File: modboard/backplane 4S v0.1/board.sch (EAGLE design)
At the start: 20 parts

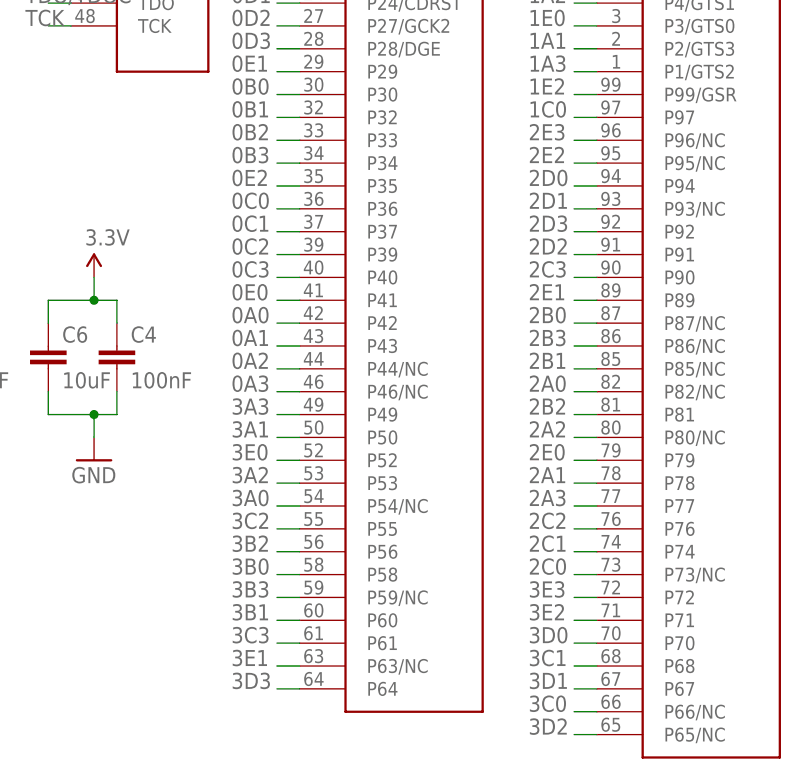
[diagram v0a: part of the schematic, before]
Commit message: rerouted parts of the modboard backplane to put the {2,3}{D,E} lanes on the NC lines
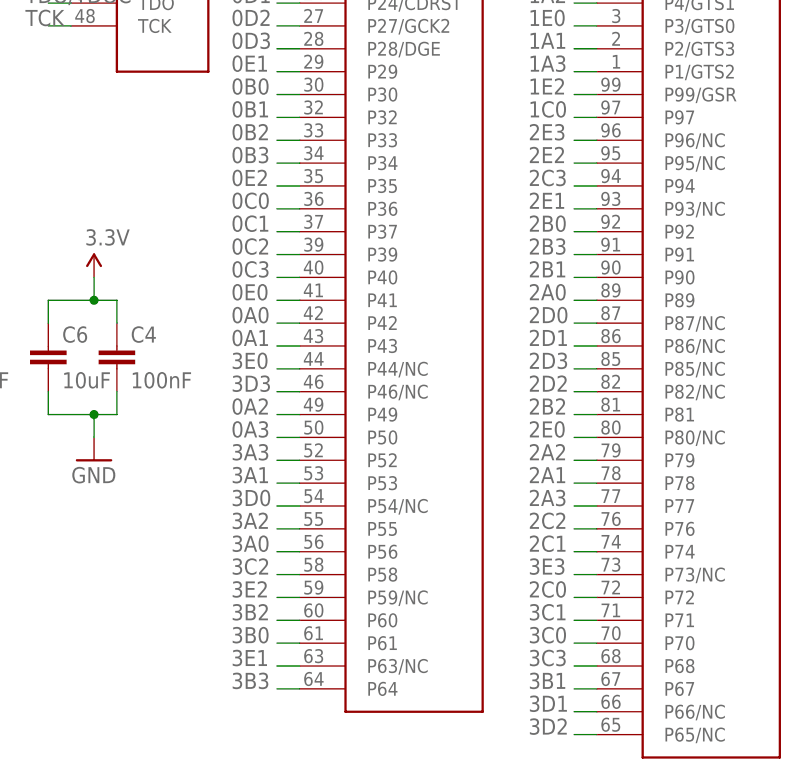
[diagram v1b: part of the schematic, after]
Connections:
- net 0A2: now also U$1.P49; no longer U$1.P44/NC
- net 0A3: now also U$1.P50; no longer U$1.P46/NC
- net 2A0: now also U$1.P89; no longer U$1.P82/NC
- net 2A2: now also U$1.P79; no longer U$1.P80/NC
- net 2B0: now also U$1.P92; no longer U$1.P87/NC
- net 2B1: now also U$1.P90; no longer U$1.P85/NC
- net 2B3: now also U$1.P91; no longer U$1.P86/NC
- net 2C0: now also U$1.P72; no longer U$1.P73/NC
- net 2C3: now also U$1.P94; no longer U$1.P90
- net 2D0: now also U$1.P87/NC; no longer U$1.P94
- net 2D1: now also U$1.P86/NC; no longer U$1.P93/NC
- net 2D2: now also U$1.P82/NC; no longer U$1.P91
- net 2D3: now also U$1.P85/NC; no longer U$1.P92
- net 2E0: now also U$1.P80/NC; no longer U$1.P79
- net 2E1: now also U$1.P93/NC; no longer U$1.P89
- net 3A0: now also U$1.P56; no longer U$1.P54/NC
- net 3A1: now also U$1.P53; no longer U$1.P50
- net 3A2: now also U$1.P55; no longer U$1.P53
- net 3A3: now also U$1.P52; no longer U$1.P49
- net 3B0: now also U$1.P61; no longer U$1.P58
- net 3B1: now also U$1.P67; no longer U$1.P60
- net 3B2: now also U$1.P60; no longer U$1.P56
- net 3B3: now also U$1.P64; no longer U$1.P59/NC
- net 3C0: now also U$1.P70; no longer U$1.P66/NC
- net 3C1: now also U$1.P71; no longer U$1.P68
- net 3C2: now also U$1.P58; no longer U$1.P55
- net 3C3: now also U$1.P68; no longer U$1.P61
- net 3D0: now also U$1.P54/NC; no longer U$1.P70
- net 3D1: now also U$1.P66/NC; no longer U$1.P67
- net 3D3: now also U$1.P46/NC; no longer U$1.P64
- net 3E0: now also U$1.P44/NC; no longer U$1.P52
- net 3E2: now also U$1.P59/NC; no longer U$1.P71
- net 3E3: now also U$1.P73/NC; no longer U$1.P72

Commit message: finished the base modboards
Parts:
- added C10, C11, C9: 100nF, kmod-passives:CAP0402-CAP
- C0: value PCIE-X1EDGE -> MB-V1-X1; device kmod-connectors:PCIE-X1EDGE -> kmod-connectors:MB-V1-X1
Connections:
- removed net 0E3: C0.B9, U$1.P22/GCK0
- removed net 1E3: C1.B9, U$1.P19
- net 0A0: now also C0.A0; no longer C0.A15
- net 0A1: now also C0.A1; no longer C0.A16
- net 0A2: now also C0.A2; no longer C0.A17
- net 0A3: now also C0.A3; no longer C0.A18
- net 0B0: now also C0.B0; no longer C0.B15
- net 0B1: now also C0.B1; no longer C0.B16
- net 0B2: now also C0.B2; no longer C0.B17
- net 0B3: now also C0.B3; no longer C0.B18
- net 0C0: now also C0.C0; no longer C0.A10
- net 0C1: now also C0.C1; no longer C0.A11
- net 0C2: now also C0.C2; no longer C0.A12
- net 0C3: now also C0.C3; no longer C0.A13
- net 0D0: now also C0.D0; no longer C0.B10
- net 0D1: now also C0.D1; no longer C0.B11
- net 0D2: now also C0.D2, U$1.P28/DGE; no longer C0.B12, U$1.P27/GCK2
- net 0D3: now also C0.D3, U$1.P29; no longer C0.B13, U$1.P28/DGE
- net 0E0: now also C0.E0, U$1.P35; no longer C0.A14, U$1.P41
- net 0E1: now also C0.E1, U$1.P22/GCK0; no longer C0.B14, U$1.P29
- net 0E2: now also C0.E2, U$1.P41; no longer C0.A9, U$1.P35
- net 1.8V: now also C0.1.8V, C11.1; no longer C0.B7
- net 12V: now also C0.12V@1, C0.12V@2; no longer C0.A8, C0.B8
- net 1A0: now also U$1.P7; no longer U$1.P6
- net 1A1: now also U$1.P3/GTS0; no longer U$1.P2/GTS3
- net 1A2: now also U$1.P6; no longer U$1.P4/GTS1
- net 1A3: now also U$1.P2/GTS3; no longer U$1.P1/GTS2
- net 1B0: now also U$1.P11; no longer U$1.P10
- net 1B1: now also U$1.P12; no longer U$1.P11
- net 1B2: now also U$1.P8; no longer U$1.P7
- net 1B3: now also U$1.P10; no longer U$1.P9
- net 1C2: now also U$1.P9; no longer U$1.P8
- net 1C3: now also U$1.P13; no longer U$1.P12
- net 1E0: now also C1.A9, U$1.P1/GTS2; no longer C1.A14, U$1.P3/GTS0
- net 1E1: now also C1.B9, U$1.P19; no longer C1.B14, U$1.P13
- net 1E2: now also C1.A14, U$1.P4/GTS1; no longer C1.A9, U$1.P99/GSR
- net 2E0: now also C2.A9, U$1.P95/NC; no longer C2.A14, U$1.P80/NC
- net 2E1: now also C2.B9, U$1.P96/NC; no longer C2.B14, U$1.P93/NC
- net 2E2: now also C2.A14, U$1.P80/NC; no longer C2.A9, U$1.P95/NC
- net 2E3: now also C2.B14, U$1.P93/NC; no longer C2.B9, U$1.P96/NC
- net 3.3V: now also C0.3.3V, C10.1, C9.1; no longer C0.A7
- net 3E0: now also C3.A9, U$1.P59/NC; no longer C3.A14, U$1.P44/NC
- net 3E1: now also C3.B9, U$1.P73/NC; no longer C3.B14, U$1.P63/NC
- net 3E2: now also C3.A14, U$1.P44/NC; no longer C3.A9, U$1.P59/NC
- net 3E3: now also C3.B14, U$1.P63/NC; no longer C3.B9, U$1.P73/NC
- net G0: now also C0.G0, U$1.P27/GCK2; no longer C0.B6
- net GND: now also C0.DSEN, C0.E3, C0.GND@1, C0.GND@2, C1.B14, C10.2, C11.2, C9.2; no longer C0.A3, C0.A4, C0.B4
- net GRST: now also C0.!GRST, U$1.P99/GSR; no longer C0.B5
- net SCL: now also C0.SCL; no longer C0.A5
- net SDA: now also C0.SDA; no longer C0.A6
- net SENSE0: now also C0.MSEN; no longer C0.B3
- net TCK: now also C0.TCK; no longer C0.B2
- net TDI: now also C0.TDI; no longer C0.B1
- net TDO/TDOC: now also C0.TDO; no longer C0.A1
- net TMS: now also C0.TMS; no longer C0.A2
